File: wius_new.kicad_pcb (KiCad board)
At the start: 2 copper layers, 105 parts, among them J1 UJ20-C-H-G-SMT-1-P16-TR, J3 1040310811, J4 SS5-10-3.00-L-D-K-TR, J8 2, J9 U.FL, SW3 Button Switch SPST-No, SW4 Button Switch SPST-No, U5 LSM6DSV, U9 PCAL6408AHK

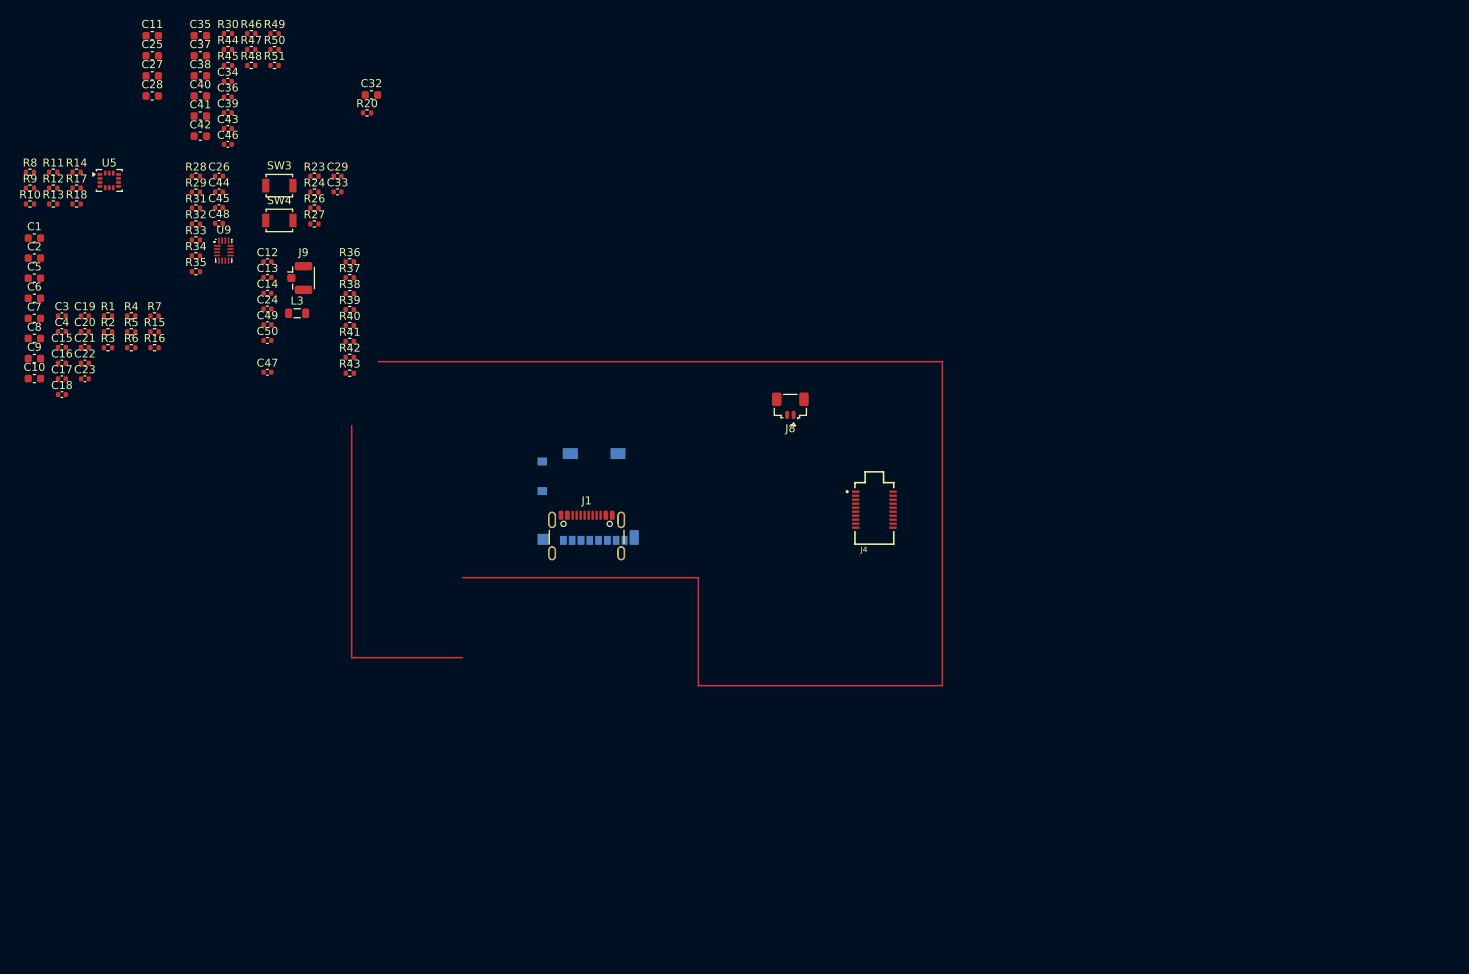
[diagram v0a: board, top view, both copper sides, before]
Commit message: changes after first review: add lvl shifters, board at 1v8, new power tree
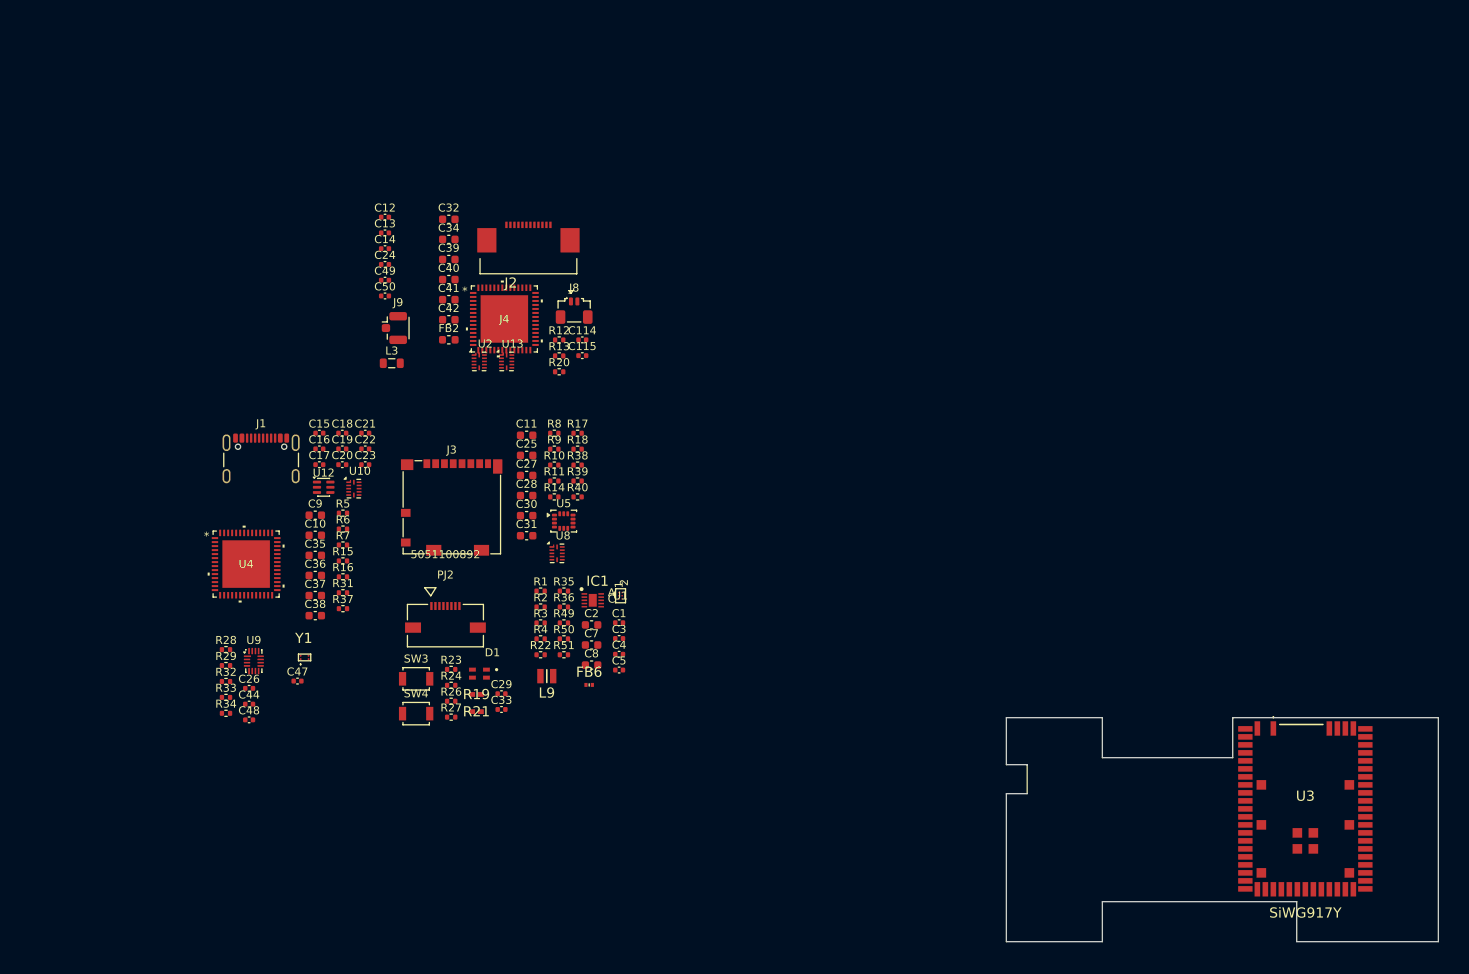
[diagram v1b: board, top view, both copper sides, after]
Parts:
- removed C43, C45, C46: 100nF, Capacitor_SMD:C_0402_1005Metric
- removed C6: 10uF, Capacitor_SMD:C_0603_1608Metric
- removed R30, R41, R42, R43: 100k, Resistor_SMD:R_0402_1005Metric
- removed R44: 267k, Resistor_SMD:R_0402_1005Metric
- removed R45, R46, R47, R48: 0, Resistor_SMD:R_0402_1005Metric
- added C114: 10uF, Capacitor_SMD:C_0402_1005Metric, F.Cu at (70.0, 38.8)
- added C115: 10uF, Capacitor_SMD:C_0402_1005Metric, F.Cu at (70.0, 40.7)
- added C30: 100nF, Capacitor_SMD:C_0603_1608Metric, F.Cu at (63.0, 60.7)
- added C31: 100nF, Capacitor_SMD:C_0603_1608Metric, F.Cu at (63.0, 63.3)
- added D1: APTB1615SURKCGKC-F01, dz_dio:LED_APTB1615SURKCGKC-F01, F.Cu at (57.1, 80.5)
- added FB2: 100Ω@100MHz, Inductor_SMD:L_0603_1608Metric, F.Cu at (53.3, 38.8)
- added FB6: 120Ω@100MHz, dz_ind:BLM15KD121SN1D, F.Cu at (70.8, 81.9)
- added IC1: BQ24040DSQT, dz_pwr:BQ24040DSQT, F.Cu at (71.3, 71.3)
- added J2: 52746-1271, dz_con:527461271, F.Cu at (63.3, 27.5)
- added L9: 2.2uH, dz_ind:DFE2MCAH2R2MJ0L, F.Cu at (65.6, 80.8)
- added PJ2: 5051100892, dz_con:CON_5051100892_MOL, F.Cu at (52.9, 74.5)
- added R19: 280, dz_res:RESC1005X40N, F.Cu at (56.8, 83.1)
- added R21: 280, dz_res:RESC1005X40N, F.Cu at (56.8, 85.2)
- added R22: 10k, Resistor_SMD:R_0402_1005Metric, F.Cu at (64.8, 78.1)
- added U1: TPS62840YBGR, dz_pwr:DSBGA6_1P4XP9_TEX, F.Cu at (74.8, 70.8)
- added U10: TXB0104RUT, Package_DFN_QFN:Texas_R-PUQFN-N12, F.Cu at (41.4, 57.4)
- added U12: SN74LVC1T45DCK, Package_TO_SOT_SMD:SOT-363_SC-70-6, F.Cu at (37.7, 57.2)
- added U13: TXB0104RUT, Package_DFN_QFN:Texas_R-PUQFN-N12, F.Cu at (60.5, 41.5)
- added U2: TXB0104RUT, Package_DFN_QFN:Texas_R-PUQFN-N12, F.Cu at (57.1, 41.5)
- added U3: SiWG917Y, dz_mcu:SiWG917Y, F.Cu at (160.4, 97.4)
- added U4: FT232HPQ, dz_comm:QFN-56_FT232HPQ_FTD, F.Cu at (28.0, 66.8)
- added U8: TXB0104RUT, Package_DFN_QFN:Texas_R-PUQFN-N12, F.Cu at (66.8, 65.5)
- added Y1: SIT1552AI-JE-DCC-32.768E, dz_sens:SIT1552AIJEDCC32768E, F.Cu at (35.3, 78.5)
- C1: value 10uF -> 1uF; footprint Capacitor_SMD:C_0603_1608Metric -> Capacitor_SMD:C_0402_1005Metric
- C3: value 100nF -> 1uF
- C34, C39: footprint Capacitor_SMD:C_0402_1005Metric -> Capacitor_SMD:C_0603_1608Metric
- C35, C37, C38, C40, C41, C42: value 10uF -> 100nF
- C36: value 470nF -> 100nF; footprint Capacitor_SMD:C_0402_1005Metric -> Capacitor_SMD:C_0603_1608Metric
- C5: value 10uF -> 100nF; footprint Capacitor_SMD:C_0603_1608Metric -> Capacitor_SMD:C_0402_1005Metric
- J3: moved to F.Cu
- J4: footprint dz_con:SAMTEC_SS5_10_3.00_X_D_K_XX -> dz_comm:QFN-56_FT232HPQ_FTD
- R1: value 270k -> 1.1k
- R12, R13, R14: value 10k -> 100k
- R2: value 0 -> 2k
- R31: value 0 -> 100k
- R35: value 22 -> 2M
- R36: value 100k -> 1M
- R37: value 0 -> 100
- moved C5 88.0 mm to (74.6, 80.0)
- moved C1 87.5 mm to (74.6, 74.1)
- moved C2 83.4 mm to (71.2, 74.4)
- moved R51 82.1 mm to (67.7, 78.1)
- moved R49 82.1 mm to (67.7, 74.2)
- moved R50 82.1 mm to (67.7, 76.1)
- moved C7 80.7 mm to (71.2, 76.9)
- moved C8 80.7 mm to (71.2, 79.4)
- moved C3 80.5 mm to (74.6, 76.1)
- moved C4 80.5 mm to (74.6, 78.1)
- moved R11 73.6 mm to (66.5, 56.4)
- moved R10 73.2 mm to (66.5, 54.4)
- moved R8 73.2 mm to (66.5, 50.4)
- moved R9 73.2 mm to (66.5, 52.4)
- moved R14 72.2 mm to (66.5, 58.4)
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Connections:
- C11 pad 1: +3V3 -> VIO
- C12 pad 1: VIO -> 3V3_VBUS
- C13 pad 1: VIO -> 3V3_VBUS
- C18 pad 1: +3V3 -> 3V3_VBUS
- C19 pad 1: +3V3 -> 3V3_VBUS
- C2 pad 1: 5V -> VBATTERY
- C20 pad 1: +3V3 -> 3V3_VBUS
- C21 pad 1: +3V3 -> 3V3_VBUS
- C22 pad 1: +3V3 -> 3V3_VBUS
- C25 pad 1: +3V3 -> VIO
- C27 pad 1: +3V3 -> 3V3_VBUS
- C28 pad 1: +3V3 -> 3V3_VBUS
- C3 pad 1: Net-(U2-EN) -> VBATTERY
- C32 pad 1: +3V3 -> VBATTERY
- C34 pad 1: VBAT -> VIO
- C35 pad 1: VSYS -> VIO
- C36 pad 1: Net-(IC1-REG) -> 3V3_VBUS
- C37 pad 1: Net-(U7-VOS) -> VIO
- C38 pad 1: Net-(U7-VOS) -> 3V3_VBUS
- C39 pad 1: Net-(U7-EN) -> VIO
- C40 pad 1: Net-(U8-VOS) -> 3V3_VBUS
- C41 pad 1: Net-(U8-VOS) -> 3V3_VBUS
- C42 pad 1: VSYS -> VIO
- C5 pad 1: Net-(U2-VOS) -> /MCU/BATT_SENSE
- J3 pad 2: /GAPmod interface/SPI_MCU.CS0 -> /IMU_SD/SPI_SD.CS0
- J3 pad 3: /GAPmod interface/SPI_MCU.MOSI -> /IMU_SD/SPI_SD.MOSI
- J3 pad 4: +3V3 -> 3V3_VBUS
- J3 pad 5: /GAPmod interface/SPI_MCU.SCK -> /IMU_SD/SPI_SD.SCK
- J3 pad 7: /GAPmod interface/SPI_MCU.MISO -> /IMU_SD/SPI_SD.MISO
- J4 pad 1: (no net) -> Net-(C114-Pad1)
- J4 pad 10: /MCU/CTRL_FPGA.INT -> /connectors/FPGA_INT
- J4 pad 12: /MCU/I2C_FG.SCL -> /MCU/LD_EN
- J4 pad 14: /MCU/CTRL_FPGA.EXT_INT_MUX -> /connectors/FPGA_EXT_INT_MUX
- J4 pad 18: /MCU/CTRL_FPGA.AFE_TX_MUX -> /connectors/FPGA_AFE_TX_MUX
- J4 pad 2: (no net) -> /connectors/FPGA_CS
- J4 pad 20: /MCU/CTRL_FPGA.RESET -> /connectors/FPGA_RESET
- J4 pad 3: (no net) -> Net-(C114-Pad1)
- J4 pad 4: (no net) -> /connectors/FPGA_MISO
- J4 pad 5: (no net) -> Net-(C114-Pad1)
- J4 pad 6: (no net) -> /connectors/FPGA_SCLK
- J4 pad 7: (no net) -> VBATTERY
- J4 pad 8: (no net) -> /connectors/FPGA_MOSI
- J4 pad 9: (no net) -> GND
- J8 pad 1: unconnected-(J8-Pin_1-Pad1) -> VBATTERY
- J8 pad 2: unconnected-(J8-Pin_2-Pad2) -> GND
- J8 pad MP: unconnected-(J8-MountPin-PadMP) -> GND
- R10 pad 1: +3V3 -> 3V3_VBUS
- R11 pad 1: +3V3 -> 3V3_VBUS
- R12 pad 1: +3V3 -> /MCU/FPGA_EN
- R12 pad 2: /GAPmod interface/SPI_MCU.CS0 -> GND
- R13 pad 1: +3V3 -> /MCU/FPGA_EN
- R13 pad 2: /GAPmod interface/SPI_MCU.MOSI -> GND
- R14 pad 1: +3V3 -> /IMU_SD/SD_EN
- R14 pad 2: /GAPmod interface/SPI_MCU.MISO -> GND
- R17 pad 1: +3V3 -> 3V3_VBUS
- R18 pad 1: +3V3 -> VIO
- R2 pad 1: 5V -> Net-(IC1-PRE-TERM)
- R2 pad 2: Net-(U2-EN) -> GND
- R20 pad 1: +3V3 -> VIO
- R3 pad 1: 5V -> VBATTERY
- R31 pad 1: /MCU/MCU_IO/SPI_FPGA.SCLK -> /MCU/FT_EN
- R31 pad 2: Net-(U6-A) -> GND
- R33 pad 1: Net-(U6-A) -> /MCU/MCU_IO/SPI_FPGA.SCLK
- R35 pad 1: /MCU/MCU_IO/SPI_FPGA.SCLK -> VBATTERY
- R35 pad 2: Net-(U6-Y) -> /MCU/BATT_SENSE
- R36 pad 1: 1V8_SW -> /MCU/BATT_SENSE
- R36 pad 2: /GAPmod interface/GAP_JTAG.NRESET -> GND
- R37 pad 1: 1V8_SW -> /USB_FT232HPQ/SPI_FT.MOSI
- R37 pad 2: Net-(PJ1-Pad1) -> /USB_FT232HPQ/SPI_FT.MISO
- R38 pad 1: Net-(P1-Pad2) -> 3V3_VBUS
- R38 pad 2: /GAPmod interface/BOOT0 -> /IMU_SD/SPI_SD.MISO
- R39 pad 1: Net-(P1-Pad3) -> 3V3_VBUS
- R39 pad 2: /GAPmod interface/BOOT0 -> /IMU_SD/SPI_SD.MOSI
- R40 pad 1: GND -> 3V3_VBUS
- R40 pad 2: /GAPmod interface/BOOT0 -> /IMU_SD/SPI_SD.CS0
- R50 pad 1: VBUS -> 3V3_VBUS
- R8 pad 1: +3V3 -> VIO
- R9 pad 1: +3V3 -> VIO
- U5 pad 12: +3V3 -> VIO
- U5 pad 2: GND -> unconnected-(U5-SDx-Pad2)
- U5 pad 3: GND -> unconnected-(U5-SCx-Pad3)
- U5 pad 5: +3V3 -> VIO
- U5 pad 8: +3V3 -> VIO
- U9 pad 2: /GAPmod interface/SPI_MCU.CS2 -> unconnected-(U9-P0-Pad2)
- U9 pad 3: /GAPmod interface/SPI_MCU.CS3 -> /IMU_SD/SPI_MCU.CS3
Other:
- board outline added: 54 x 28 mm
- copper layers 2 -> 6

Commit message: updated schematic and initial pcb placement
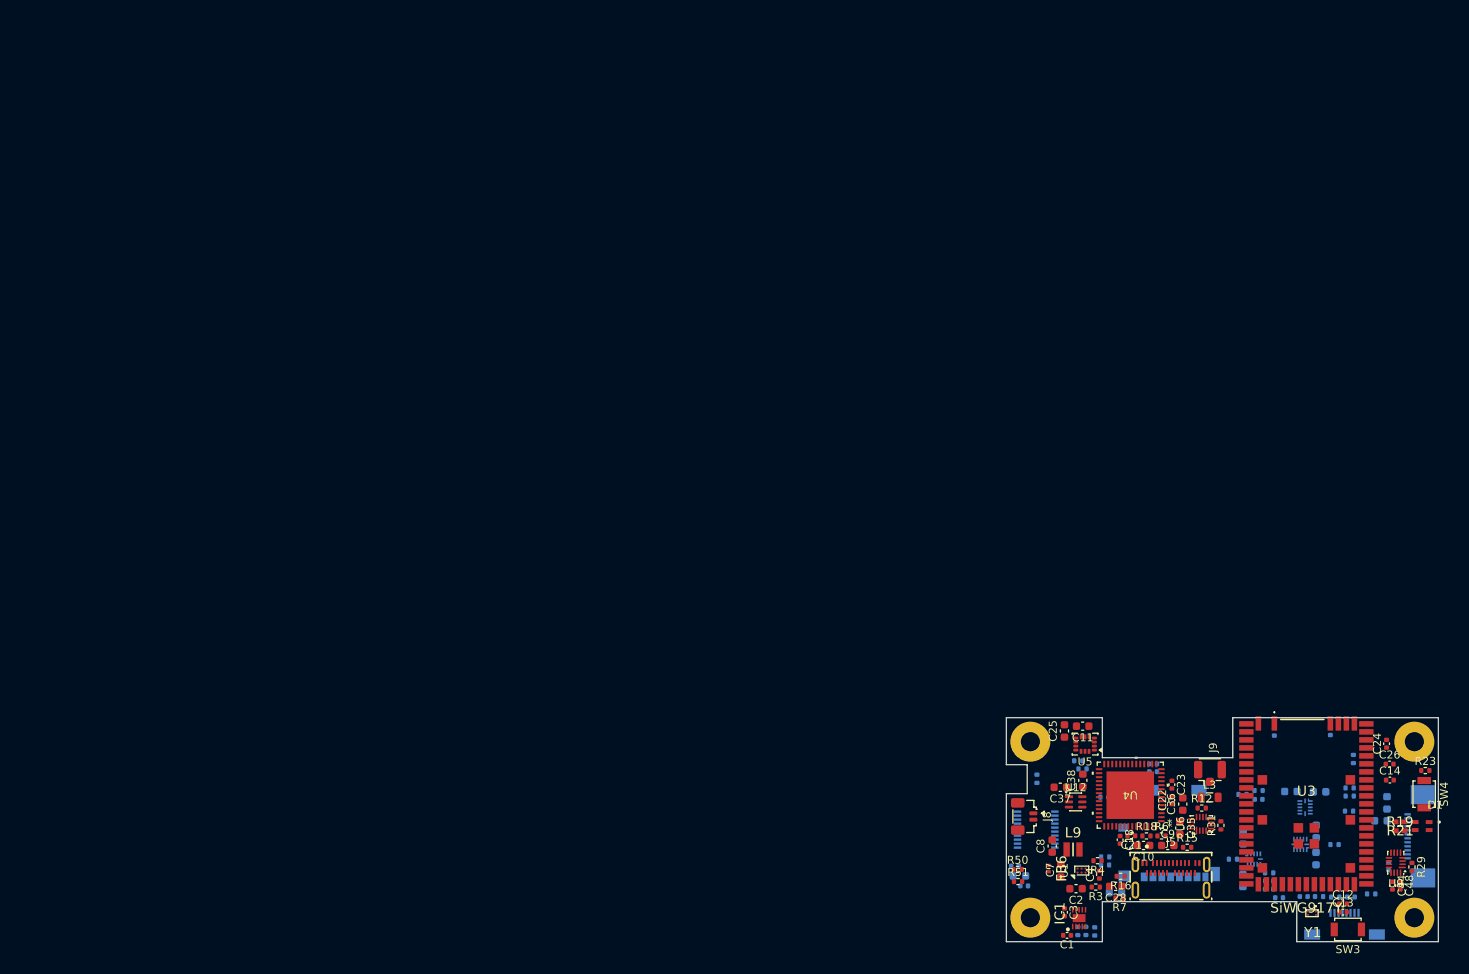
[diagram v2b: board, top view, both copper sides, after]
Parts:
- removed C15, C17: 100nF, Capacitor_SMD:C_0402_1005Metric
- removed C16: 4.7uF, Capacitor_SMD:C_0402_1005Metric
- removed J1: UJ20-C-H-G-SMT-1-P16-TR, Connector_USB:USB_C_Receptacle_GCT_USB4105-xx-A_16P_TopMnt_Horizontal
- removed R36: 1M, Resistor_SMD:R_0402_1005Metric
- removed R37: 100, Resistor_SMD:R_0402_1005Metric
- removed R49: 0, Resistor_SMD:R_0402_1005Metric
- removed R5: 6.8k, Resistor_SMD:R_0402_1005Metric
- removed U10: TXB0104RUT, Package_DFN_QFN:Texas_R-PUQFN-N12
- added J5: USB4745-03-A, dz_con:GTC_USB4745, F.Cu at (143.6, 109.0)
- added M1: MountingHole_Pad, dz_mech:MountingHole_2.4mm_M2_Pad_TopBottom, F.Cu at (126.0, 111.0)
- added M2: MountingHole_Pad, dz_mech:MountingHole_2.4mm_M2_Pad_TopBottom, F.Cu at (126.0, 89.0)
- added M3: MountingHole_Pad, dz_mech:MountingHole_2.4mm_M2_Pad_TopBottom, F.Cu at (174.0, 89.0)
- added M4: MountingHole_Pad, dz_mech:MountingHole_2.4mm_M2_Pad_TopBottom, F.Cu at (174.0, 111.0)
- added R25: 100k, Resistor_SMD:R_0402_1005Metric, B.Cu at (126.8, 93.6)
- added R30: 100k, Resistor_SMD:R_0402_1005Metric, B.Cu at (154.5, 95.1)
- added U6: SN74AXC4T774RSVR, Package_DFN_QFN:UQFN-16_1.8x2.6mm_P0.4mm, F.Cu at (147.4, 99.3)
- C114, C115, C19, C20, C27, C29, C30, C31, C32, C33, C34, C39, C40, C41, C42, C47, C49, C5, C50, FB2, J2, J3, PJ2, R1, R10, R11, R13, R14, R17, R2, R20, R22, R24, R26, R27, R28, R32, R33, R34, R38, R39, R40, R8, R9, U13, U2, U8: moved to B.Cu
- J4: footprint dz_comm:QFN-56_FT232HPQ_FTD -> dz_con:SAMTEC_SS5_10_3.00_X_D_K_XX; moved to B.Cu
- R12: value 100k -> 1k
- R18: value 10k -> 6.65k
- R35: value 2M -> 220k; moved to B.Cu
- U1: footprint dz_pwr:DSBGA6_1P4XP9_TEX -> Package_BGA:Texas_DSBGA-6_0.9x1.4mm_Layout2x3_P0.5mm
- moved R29 150.4 mm to (173.7, 104.7), turned to -90 degrees
- moved C12 147.3 mm to (165.1, 109.3)
- moved C13 146.8 mm to (165.1, 110.3)
- moved C48 145.4 mm to (172.2, 107.0), turned to -90 degrees
- moved U9 144.9 mm to (171.7, 104.1), turned to 180 degrees
- moved C44 144.7 mm to (171.3, 107.0), turned to -90 degrees
- moved C26 142.9 mm to (170.9, 91.8)
- moved C14 142.1 mm to (170.9, 93.8)
- moved R28 141.6 mm to (166.4, 91.2), turned to 90 degrees
- moved R32 141.3 mm to (165.8, 97.7)
- moved R33 140.9 mm to (165.9, 94.8)
- moved R34 140.8 mm to (165.9, 95.8)
- moved C24 138.8 mm to (170.5, 89.2), turned to 90 degrees
- moved C32 138.1 mm to (170.6, 96.7), turned to 90 degrees
- moved C34 137.3 mm to (169.8, 98.9), turned to 180 degrees
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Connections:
- J2 pad 10: /IMU_SD/SPI_MCU.MISO -> /MCU/ULP_SSI.MISO
- J2 pad 11: /IMU_SD/SPI_MCU.MOSI -> /MCU/ULP_SSI.MOSI
- J2 pad 7: /IMU_SD/SPI_MCU.CS3 -> /MCU/ULP_SSI.CS0
- J2 pad 8: /IMU_SD/SPI_MCU.SCK -> /MCU/ULP_SSI.SCK
- J4 pad 12: /MCU/LD_EN -> /connectors/LD_EN
- R12 pad 1: /MCU/FPGA_EN -> /USB_FT232HPQ/SPI_FT.MOSI
- R12 pad 2: GND -> /USB_FT232HPQ/SPI_FT232.MIOSI0
- R18 pad 1: VIO -> 5V
- R18 pad 2: /IMU_SD/INT_IMU -> Net-(U4A-PD1_SVBUS)
- R31 pad 1: /MCU/FT_EN -> VIO
- R31 pad 2: GND -> /MCU/FT_EN
- R33 pad 1: /MCU/MCU_IO/SPI_FPGA.SCLK -> /MCU/SPI_FPGA.SCK
- U13 pad 10: /connectors/FPGA_INT -> /connectors/FPGA_RESET
- U13 pad 2: /MCU/CTRL_FPGA.INT -> /MCU/CTRL_FPGA.RESET
- U13 pad 3: /MCU/CTRL_FPGA.EXT_INT_MUX -> /MCU/CTRL_FPGA.AFE_TX_MUX
- U13 pad 4: /MCU/CTRL_FPGA.AFE_TX_MUX -> /MCU/CTRL_FPGA.EXT_INT_MUX
- U13 pad 5: /MCU/CTRL_FPGA.RESET -> /MCU/CTRL_FPGA.INT
- U13 pad 7: /connectors/FPGA_RESET -> /connectors/FPGA_INT
- U13 pad 8: /connectors/FPGA_AFE_TX_MUX -> /connectors/FPGA_EXT_INT_MUX
- U13 pad 9: /connectors/FPGA_EXT_INT_MUX -> /connectors/FPGA_AFE_TX_MUX
- U2 pad 10: /connectors/FPGA_SCLK -> /connectors/FPGA_MISO
- U2 pad 2: /connectors/SPI_FPGA.SCLK -> /MCU/SPI_FPGA.MISO
- U2 pad 3: /MCU/SPI_FPGA.MOSI -> /MCU/SPI_FPGA.SCK
- U2 pad 4: /MCU/SPI_FPGA.MISO -> /MCU/SPI_FPGA.CS0
- U2 pad 5: /MCU/SPI_FPGA.CS0 -> /MCU/SPI_FPGA.MOSI
- U2 pad 7: /connectors/FPGA_CS -> /connectors/FPGA_MOSI
- U2 pad 8: /connectors/FPGA_MISO -> /connectors/FPGA_CS
- U2 pad 9: /connectors/FPGA_MOSI -> /connectors/FPGA_SCLK
- U3 pad 19: /MCU/FT_EN -> /IMU_SD/SPI_MCU.CS1
- U3 pad 39: unconnected-(U3C-GPIO_48-Pad39) -> /MCU/ULP_SSI.CS0
- U3 pad 40: unconnected-(U3C-GPIO_47-Pad40) -> /MCU/ULP_SSI.MISO
- U3 pad 41: unconnected-(U3C-GPIO_49-Pad41) -> /MCU/ULP_SSI.MOSI
- U3 pad 44: unconnected-(U3C-GPIO_46-Pad44) -> /MCU/ULP_SSI.SCK
- U3 pad 55: /IMU_SD/SPI_MCU.CS1 -> /MCU/FT_EN
- U3 pad 56: /MCU/LD_EN -> unconnected-(U3C-GPIO_12-Pad56)
- U4 pad 23: /USB_FT232HPQ/SPI_FT.MISO -> /USB_FT232HPQ/SPI_FT232.MIOSI0
- U9 pad 3: /IMU_SD/SPI_MCU.CS3 -> unconnected-(U9-P1-Pad3)
